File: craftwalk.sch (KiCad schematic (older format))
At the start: 31 parts, among them J1 LED, SW1 RESET_SW, U1 ProMicro

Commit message: precreate
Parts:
- MX12: footprint MX_Only:MXOnly-1U-NoLED -> MX_Only:MXOnly-1U-Hotswap
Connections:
- net COL0: now also U1.16 (B1/15); no longer U1.20 (F4/A3)
- net COL1: now also U1.17 (F7/A0); no longer U1.19 (F5/A2)
- net COL2: now also U1.19 (F5/A2); no longer U1.18 (F6/A1)
- net COL3: now also U1.20 (F4/A3); no longer U1.17 (F7/A0)
- net COL4: no longer D4.1 (K), D5.1 (K), D6.1 (K), D7.1 (K), MX13.1 (COL), MX14.1 (COL), U1.15 (B3/14), U1.16 (B1/15), U1.8 (5/C6)
- net ROW0: now also U1.18 (F6/A1); no longer U1.7 (4/D4)
- net ROW2: now also U1.12 (9/B5); no longer U1.9 (6/D7)
- net COL5: now reaches U1.10 (7/E6)
- net COL5: now also MX13.1 (COL)
- net COL6: now reaches U1.11 (8/B4)
- net COL6: now also MX14.1 (COL)
- new net ROW1: D4.1 (K), D5.1 (K), D6.1 (K), D7.1 (K), U1.15 (B3/14)
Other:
- note added: "1"
- note added: "1.0\n"
- note added: "2019-12-08"
- note added: "MCU"
- note added: "Switch"
- note added: "craftWalk by sotoba"
- note added: "miscellaneous"
- moved on the sheet: J1, SW1, U1

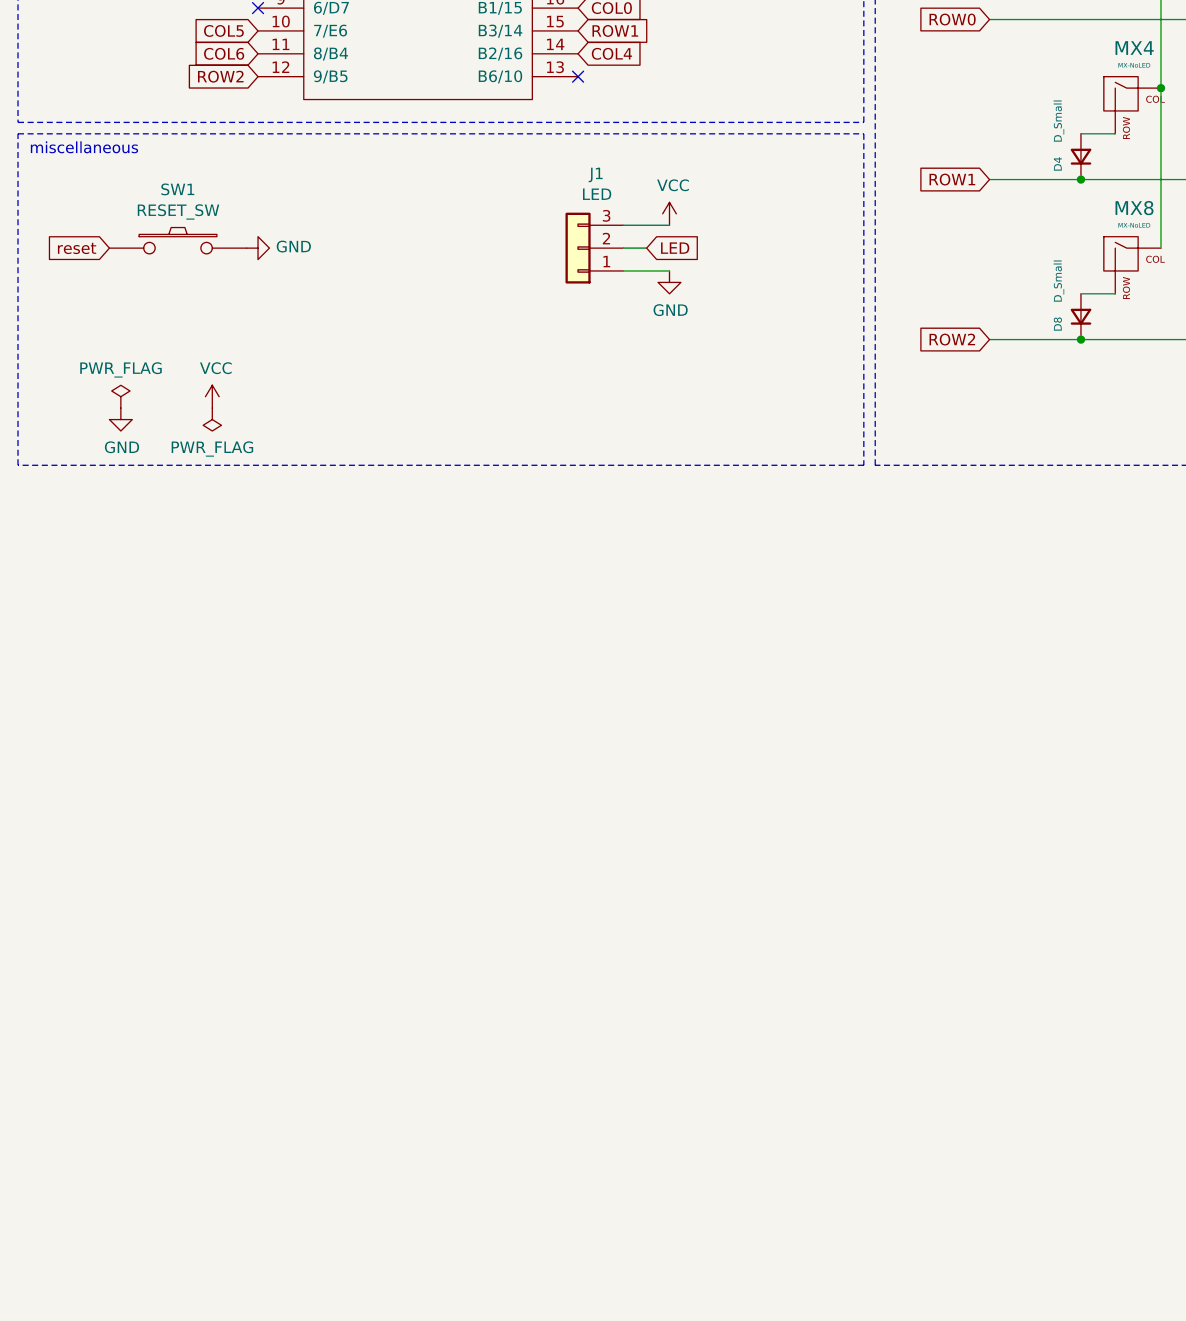
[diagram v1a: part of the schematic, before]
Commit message: rev 1.2
- add LED support
- change libs to submodule
- refactor
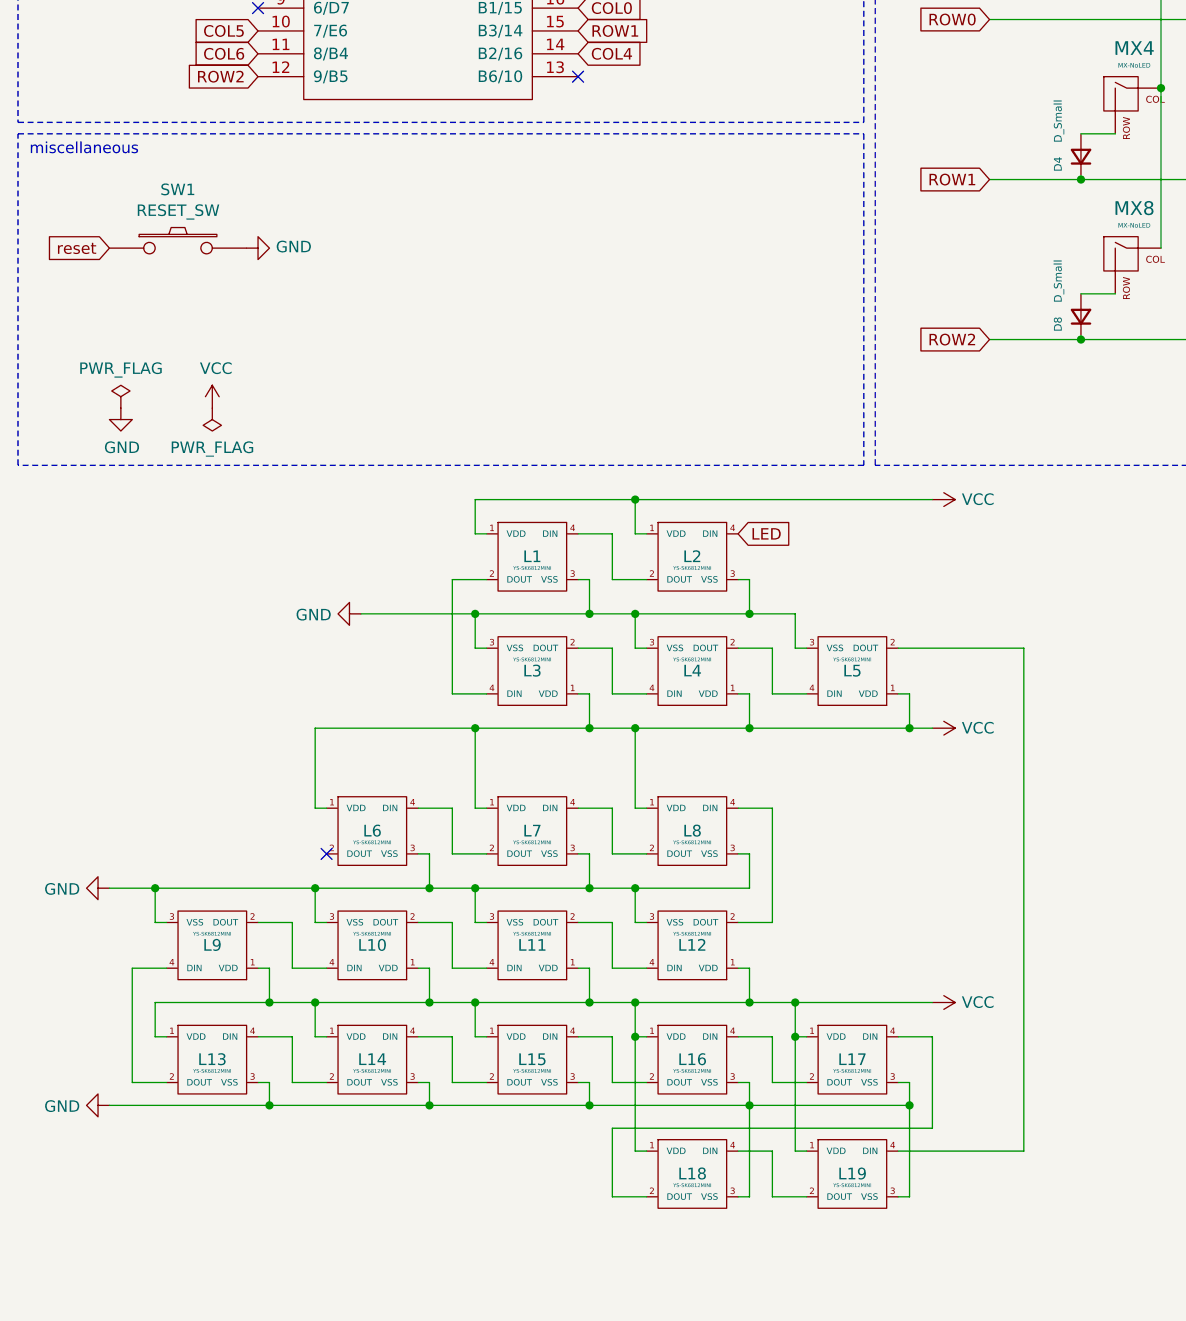
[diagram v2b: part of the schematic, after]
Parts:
- removed J1: LED, kbd:StripLED_rev, symbol Connector_Generic:Conn_01x03
- added L1, L2, L3, L4, L5: YS-SK6812MINI, craftwalk:YS-SK6812, symbol kbd:YS-SK6812MINI
- added L10, L11, L12, L13, L14, L15, L16, L17, L18, L19, L6, L7, L8, L9: YS-SK6812MINI, craftwalk:YS-SK6812-underglow, symbol kbd:YS-SK6812MINI
- SW1: footprint Keebio-Parts:SW_Tactile_SPST_Angled_MJTP1117 -> random-keyboard-parts:SKQGADE010
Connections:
- net GND: now also L1.3 (VSS), L10.3 (VSS), L11.3 (VSS), L12.3 (VSS), L13.3 (VSS), L14.3 (VSS), L15.3 (VSS), L16.3 (VSS), L17.3 (VSS), L18.3 (VSS), L19.3 (VSS), L2.3 (VSS), L3.3 (VSS), L4.3 (VSS), L5.3 (VSS), L6.3 (VSS), L7.3 (VSS), L8.3 (VSS), L9.3 (VSS)
- net LED: now also L2.4 (DIN)
- net VCC: now also L1.1 (VDD), L10.1 (VDD), L11.1 (VDD), L12.1 (VDD), L13.1 (VDD), L14.1 (VDD), L15.1 (VDD), L16.1 (VDD), L17.1 (VDD), L18.1 (VDD), L19.1 (VDD), L2.1 (VDD), L3.1 (VDD), L4.1 (VDD), L5.1 (VDD), L6.1 (VDD), L7.1 (VDD), L8.1 (VDD), L9.1 (VDD)
- new net: L1.2 (DOUT), L3.4 (DIN)
- new net: L1.4 (DIN), L2.2 (DOUT)
- new net: L3.2 (DOUT), L4.4 (DIN)
- new net: L4.2 (DOUT), L5.4 (DIN)
- new net: L19.4 (DIN), L5.2 (DOUT)
- new net: L7.4 (DIN), L8.2 (DOUT)
- new net: L12.2 (DOUT), L8.4 (DIN)
- new net: L6.4 (DIN), L7.2 (DOUT)
- new net: L10.4 (DIN), L9.2 (DOUT)
- new net: L13.2 (DOUT), L9.4 (DIN)
- new net: L10.2 (DOUT), L11.4 (DIN)
- new net: L11.2 (DOUT), L12.4 (DIN)
- new net: L13.4 (DIN), L14.2 (DOUT)
- new net: L14.4 (DIN), L15.2 (DOUT)
- new net: L15.4 (DIN), L16.2 (DOUT)
- new net: L16.4 (DIN), L17.2 (DOUT)
- new net: L17.4 (DIN), L18.2 (DOUT)
- new net: L18.4 (DIN), L19.2 (DOUT)
- no-connect marks 8 -> 9

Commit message: fix symbol link
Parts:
- L1, L10, L11, L12, L13, L14, L15, L16, L17, L18, L19, L2, L3, L4, L5, L6, L7, L8, L9: symbol kbd:YS-SK6812MINI -> craftwalk:YS-SK6812MINI-kbd
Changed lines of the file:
@@
 miscellaneous
 $Comp
-L kbd:YS-SK6812MINI L1
+L craftwalk:YS-SK6812MINI-kbd L1
 U 1 1 5E1ABC04
 P 2850 4400
@@
 $EndComp
 $Comp
-L kbd:YS-SK6812MINI L2
+L craftwalk:YS-SK6812MINI-kbd L2
 U 1 1 5E1F281F
 P 3550 4400
@@
 $EndComp
 $Comp
-L kbd:YS-SK6812MINI L3
+L craftwalk:YS-SK6812MINI-kbd L3
 U 1 1 5E1F361C
 P 2850 4900
@@
 $EndComp
 $Comp
-L kbd:YS-SK6812MINI L4
+L craftwalk:YS-SK6812MINI-kbd L4
 U 1 1 5E1F3EEC
 P 3550 4900
@@
 $EndComp
 $Comp
-L kbd:YS-SK6812MINI L5
+L craftwalk:YS-SK6812MINI-kbd L5
 U 1 1 5E1F43D4
 P 4250 4900
@@
 $EndComp
 $Comp
-L kbd:YS-SK6812MINI L8
+L craftwalk:YS-SK6812MINI-kbd L8
 U 1 1 5E2656EE
 P 3550 5600
@@
 $EndComp
 $Comp
-L kbd:YS-SK6812MINI L7
+L craftwalk:YS-SK6812MINI-kbd L7
 U 1 1 5E265F28
 P 2850 5600
@@
 $EndComp
 $Comp
-L kbd:YS-SK6812MINI L6
+L craftwalk:YS-SK6812MINI-kbd L6
 U 1 1 5E2665EB
 P 2150 5600
@@
 $EndComp
 $Comp
-L kbd:YS-SK6812MINI L9
+L craftwalk:YS-SK6812MINI-kbd L9
 U 1 1 5E27627E
 P 1450 6100
@@
 	2500 5500 2350 5500
 $Comp
-L kbd:YS-SK6812MINI L10
+L craftwalk:YS-SK6812MINI-kbd L10
 U 1 1 5E3B55BD
 P 2150 6100
@@
 $EndComp
 $Comp
-L kbd:YS-SK6812MINI L11
+L craftwalk:YS-SK6812MINI-kbd L11
 U 1 1 5E3BF8B4
 P 2850 6100
@@
 $EndComp
 $Comp
-L kbd:YS-SK6812MINI L12
+L craftwalk:YS-SK6812MINI-kbd L12
 U 1 1 5E3C01B6
 P 3550 6100
@@
 $EndComp
 $Comp
-L kbd:YS-SK6812MINI L13
+L craftwalk:YS-SK6812MINI-kbd L13
 U 1 1 5E468531
 P 1450 6600
@@
 $EndComp
 $Comp
-L kbd:YS-SK6812MINI L14
+L craftwalk:YS-SK6812MINI-kbd L14
 U 1 1 5E468F8B
 P 2150 6600
@@
 $EndComp
 $Comp
-L kbd:YS-SK6812MINI L15
+L craftwalk:YS-SK6812MINI-kbd L15
 U 1 1 5E469B49
 P 2850 6600
@@
 $EndComp
 $Comp
-L kbd:YS-SK6812MINI L16
+L craftwalk:YS-SK6812MINI-kbd L16
 U 1 1 5E46A590
 P 3550 6600
@@
 $EndComp
 $Comp
-L kbd:YS-SK6812MINI L17
+L craftwalk:YS-SK6812MINI-kbd L17
 U 1 1 5E46AD66
 P 4250 6600
@@
 $EndComp
 $Comp
-L kbd:YS-SK6812MINI L18
+L craftwalk:YS-SK6812MINI-kbd L18
 U 1 1 5E46BEDD
 P 3550 7100
@@
 $EndComp
 $Comp
-L kbd:YS-SK6812MINI L19
+L craftwalk:YS-SK6812MINI-kbd L19
 U 1 1 5E46CFC8
 P 4250 7100
